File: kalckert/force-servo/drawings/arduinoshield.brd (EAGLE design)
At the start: 100 x 80 mm, 20 parts, among them IC1 MCP604P, IC2 7806L

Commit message: Finnished PC board
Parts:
- added X3, X4: (no value), con-phoenix-254:2POL254
- moved C1 33.2 mm to (56.1, 8.38), turned to 180 degrees
- moved SG1 30.9 mm to (40.4, 38.7), turned to 90 degrees
- moved C4 28.9 mm to (34.4, 8.38), turned to 90 degrees
- moved C3 28.6 mm to (45.7, 8.38), turned to 90 degrees
- moved C2 26.3 mm to (56.1, 21.5)
- moved POWERPIN 26.2 mm to (36.8, 2.54)
- moved IC2 26.0 mm to (40.0, 7.11)
- moved DIGITALPIN0-7 25.7 mm to (54.6, 50.8)
- moved DIGITALPIN8+ 25.6 mm to (30.2, 50.8)
- moved ANALOGPIN 25.3 mm to (57.1, 2.54)
- moved BATTERY 23.1 mm to (62.1, 9.91)
- moved 7905 20.3 mm to (57.4, 14.2), turned to 90 degrees
- moved X2 20.1 mm to (62.1, 29.5)
- moved X1 18.8 mm to (62.1, 23.1)
- moved SERVOPIN 15.1 mm to (63.5, 42.7)
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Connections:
- net GND: now also X3.1, X4.1
- net LED_GREEN: now also X3.2
- net LED_RED: now also X4.2
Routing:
- net GND: track 0.00 -> 151.0 mm
- net AMP_FORCE1: track 0.00 -> 77.6 mm
- net FORCE1: track 0.00 -> 62.4 mm
- net AMP_FORCE2: track 0.00 -> 57.5 mm
- net SERVOPOS: track 0.00 -> 52.8 mm, vias 0 -> 1
- net LED_RED: track 0.00 -> 49.8 mm
- net VCCSERVO: track 0.00 -> 48.5 mm
- net FORCE2: track 0.00 -> 46.0 mm
- net LED_GREEN: track 0.00 -> 45.9 mm
- net -9V: track 0.00 -> 42.3 mm
- net 5V: track 0.00 -> 39.2 mm
- net SERVOPWM: track 0.00 -> 37.7 mm
- net N$3: track 0.00 -> 18.7 mm
- net N$2: track 0.00 -> 16.3 mm
- net BUZZER: track 0.00 -> 10.4 mm
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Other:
- outline, holes or cut-outs redrawn

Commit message: First version of the PCB is ready.
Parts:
- removed 7905: 7905, linear:TO92
- removed IC2: 7806L, linear:TO92
- added IC3: 7806T, linear:TO220H
- added IC4: (no value), linear:TO220H
- moved R1 46.3 mm to (53.2, 12.6), turned to 90 degrees
- moved R4 39.7 mm to (15.2, 36.3), turned to 180 degrees
- moved R3 34.9 mm to (15.4, 42.7), turned to 180 degrees
- moved SERVOPIN 34.7 mm to (29.7, 34.8), turned to 180 degrees
- moved R2 32.7 mm to (50.7, 27.7), turned to 270 degrees
- moved C2 30.5 mm to (25.9, 17.3), turned to 90 degrees
- moved C1 30.4 mm to (25.9, 11.8), turned to 90 degrees
- moved C3 24.4 mm to (26.0, 22.9)
- moved C4 21.6 mm to (26.0, 28.3), turned to 270 degrees
- moved IC1 21.3 mm to (43.2, 20.1), turned to 90 degrees
- moved SG1 17.8 mm to (57.9, 41.7)
- moved BATTERY 3.06 mm to (62.4, 13.0)
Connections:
- net -9V: now also IC4.1; no longer 7905.1
- net BUZZER: now also DIGITALPIN0-7.4; no longer DIGITALPIN0-7.1
- net GND: now also IC4.3; no longer 7905.3
- net N$1: now also DIGITALPIN0-7.1; no longer DIGITALPIN0-7.3
- net N$2: now also IC4.2; no longer 7905.2
- net N$3: now also IC3.2; no longer IC2.2
- net N$4: now also DIGITALPIN0-7.2; no longer DIGITALPIN0-7.4
- net VCCSERVO: now also IC3.3; no longer IC2.1
- net VIN: now also IC3.1; no longer IC2.3
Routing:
- net N$4: track 5.89 -> 74.0 mm
- net AMP_FORCE1: track 77.6 -> 15.9 mm
- net VIN: track 5.08 -> 50.9 mm
- net LED_RED: track 49.8 -> 4.18 mm
- net LED_GREEN: track 45.9 -> 4.33 mm
- net FORCE1: track 62.4 -> 21.8 mm
- net -9V: track 42.3 -> 81.7 mm
- net VCCSERVO: track 48.5 -> 12.4 mm
- net FORCE2: track 46.0 -> 16.6 mm
- net N$2: track 16.3 -> 42.5 mm
- net N$1: track 5.65 -> 29.9 mm
- net SERVOPOS: track 52.8 -> 76.6 mm, vias 1 -> 0
- net AMP_FORCE2: track 57.5 -> 38.7 mm
- net 5V: track 39.2 -> 22.1 mm
- net N$3: track 18.7 -> 6.13 mm
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- added copper zone on layer 1, net N$8
- added copper zone on layer 16, net N$9
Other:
- board text added: "AlexDesign"

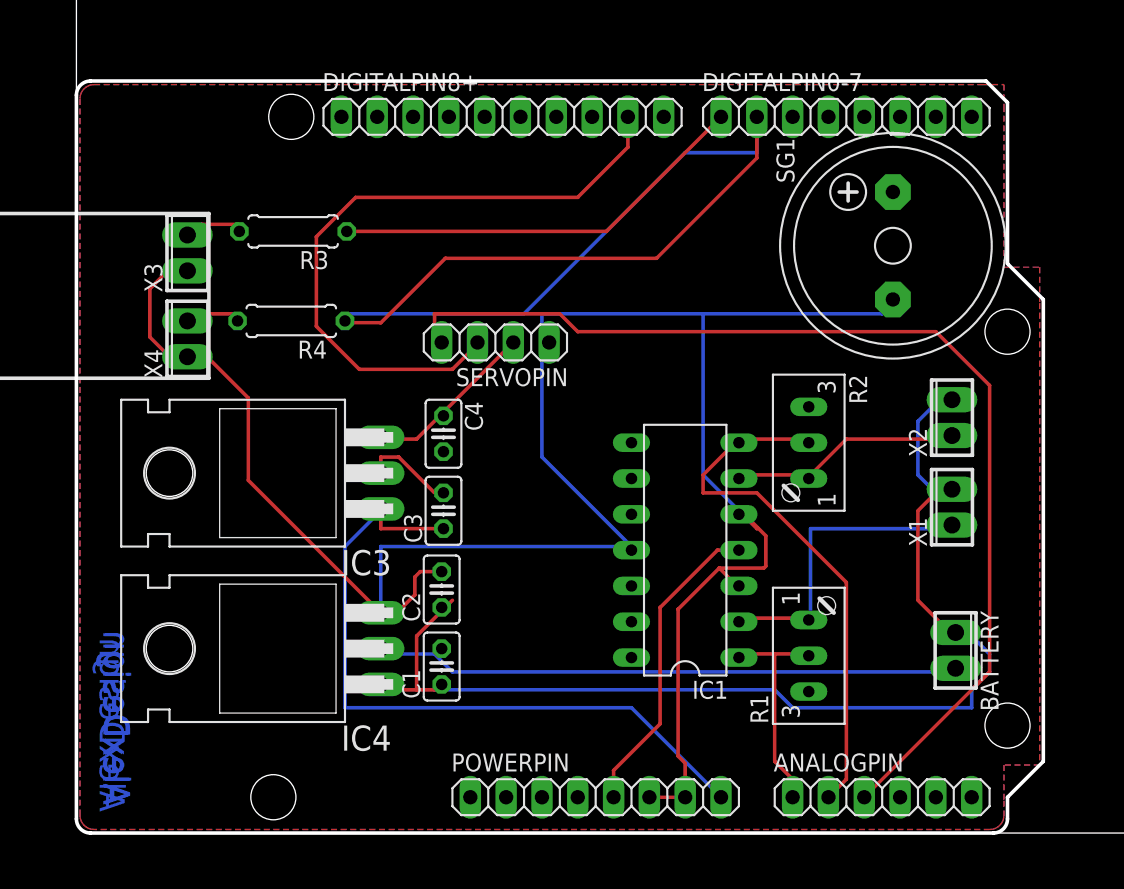
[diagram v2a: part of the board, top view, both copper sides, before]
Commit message: Added licensing info to board. Tested python program on mac (tkinter only works in IDLE).
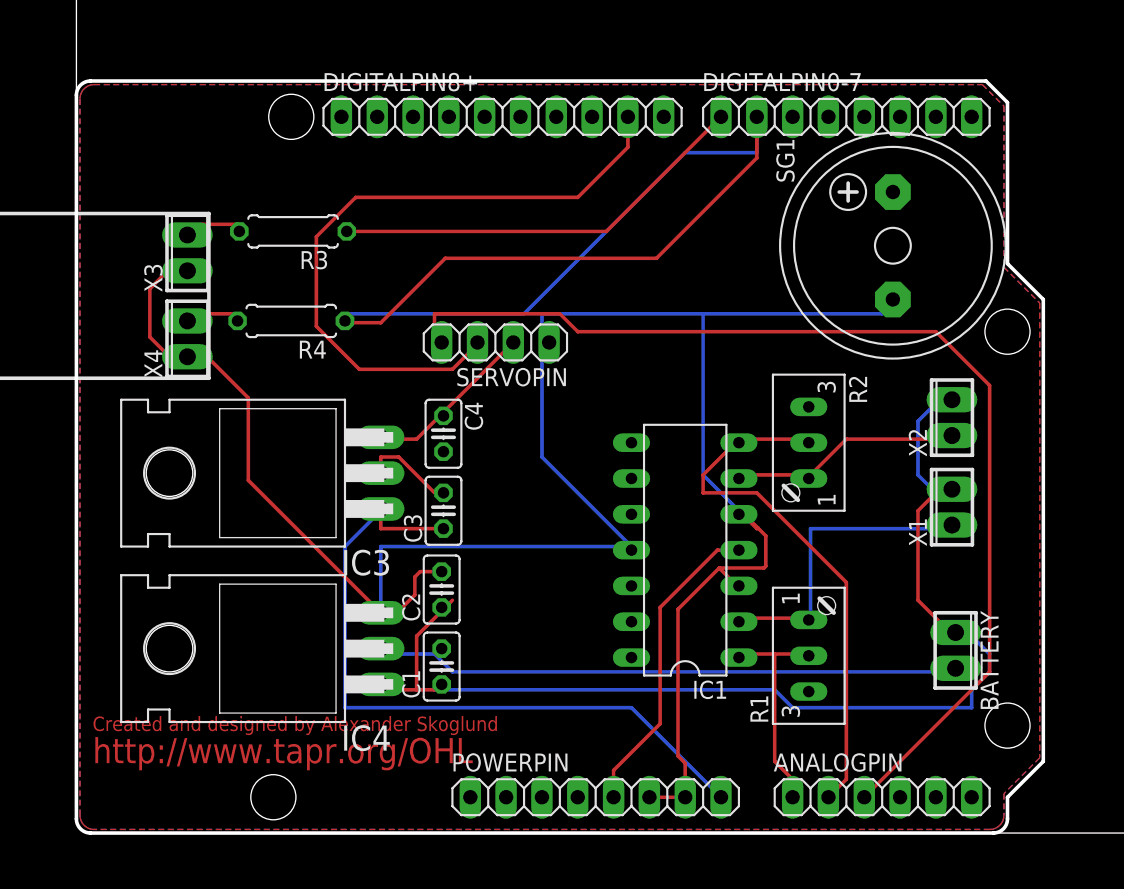
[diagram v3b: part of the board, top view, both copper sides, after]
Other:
- board text added: "Created and designed by Alexander Skoglund"
- board text added: "http://www.tapr.org/OHL"
- board text removed: "AlexDesign"
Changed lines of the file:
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@@
 <layer number="17" name="Pads" color="2" fill="1" visible="yes" active="yes"/>
 <layer number="18" name="Vias" color="2" fill="1" visible="yes" active="yes"/>
-<layer number="19" name="Unrouted" color="6" fill="1" visible="no" active="yes"/>
+<layer number="19" name="Unrouted" color="6" fill="1" visible="yes" active="yes"/>
 <layer number="20" name="Dimension" color="15" fill="1" visible="yes" active="yes"/>
-<layer number="21" name="tPlace" color="7" fill="1" visible="no" active="yes"/>
+<layer number="21" name="tPlace" color="7" fill="1" visible="yes" active="yes"/>
 <layer number="22" name="bPlace" color="7" fill="1" visible="no" active="yes"/>
-<layer number="23" name="tOrigins" color="15" fill="1" visible="no" active="yes"/>
-<layer number="24" name="bOrigins" color="15" fill="1" visible="no" active="yes"/>
-<layer number="25" name="tNames" color="7" fill="1" visible="no" active="yes"/>
-<layer number="26" name="bNames" color="7" fill="1" visible="no" active="yes"/>
+<layer number="23" name="tOrigins" color="15" fill="1" visible="yes" active="yes"/>
+<layer number="24" name="bOrigins" color="15" fill="1" visible="yes" active="yes"/>
+<layer number="25" name="tNames" color="7" fill="1" visible="yes" active="yes"/>
+<layer number="26" name="bNames" color="7" fill="1" visible="yes" active="yes"/>
 <layer number="27" name="tValues" color="7" fill="1" visible="no" active="yes"/>
 <layer number="28" name="bValues" color="7" fill="1" visible="no" active="yes"/>
@@
 <wire x1="9.398" y1="32.258" x2="-6.35" y2="32.258" width="0.254" layer="21"/>
 <wire x1="-6.35" y1="32.258" x2="-6.35" y2="43.942" width="0.254" layer="21"/>
-<text x="3.81" y="14.351" size="1.778" layer="16" rot="MR270">AlexDesign</text>
-<text x="3.683" y="14.351" size="1.778" layer="16" rot="MR270">AlexDesign</text>
-<text x="3.429" y="13.843" size="1.778" layer="16" rot="MR270">AlexDesign</text>
+<text x="1.143" y="4.953" size="1.778" layer="1">http://www.tapr.org/OHL</text>
+<text x="1.143" y="7.239" size="1.016" layer="1">Created and designed by Alexander Skoglund</text>
 </plain>
 <attributes>
@@
 <vertex x="1.254" y="53.086"/>
 <vertex x="64.262" y="53.086"/>
-<vertex x="65.786" y="53.086"/>
 <vertex x="65.786" y="51.562"/>
 <vertex x="65.786" y="40.132"/>
-<vertex x="68.326" y="40.132"/>
 <vertex x="68.326" y="37.592"/>
-<vertex x="68.326" y="4.826"/>
-<vertex x="65.786" y="4.826"/>
-<vertex x="65.786" y="2.286"/>
+<vertex x="68.326" y="5.334"/>
+<vertex x="65.786" y="2.794"/>
 <vertex x="65.786" y="1.254" curve="-90"/>
 <vertex x="64.786" y="0.254"/>
@@
 <vertex x="1.254" y="53.086"/>
 <vertex x="64.262" y="53.086"/>
-<vertex x="65.786" y="53.086"/>
 <vertex x="65.786" y="51.562"/>
 <vertex x="65.786" y="40.132"/>
-<vertex x="68.326" y="40.132"/>
 <vertex x="68.326" y="37.592"/>
-<vertex x="68.326" y="4.826"/>
-<vertex x="65.786" y="4.826"/>
-<vertex x="65.786" y="2.286"/>
+<vertex x="68.326" y="5.334"/>
+<vertex x="65.786" y="2.794"/>
 <vertex x="65.786" y="1.254" curve="-90"/>
 <vertex x="64.786" y="0.254"/>

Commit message: Added a timestamp to the measure, ms from start of prog.
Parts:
- added SG2: EFBRD22C41, buzzer:EFBRD22C41
- added SG3: EFBAA40D101, buzzer:EFBAA40D101
- added SG4: F/QMX, buzzer:F/QMX
- added SG5: EFBRD22C413, buzzer:EFBRD22C413
- added SG6: EFBRD24C411, buzzer:EFBRD24C411
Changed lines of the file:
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@@
 <element name="IC3" library="linear" package="TO220H" value="7806T" x="11.43" y="25.527" rot="R90"/>
 <element name="IC4" library="linear" package="TO220H" value="" x="11.43" y="13.081" rot="R90"/>
+<element name="SG4" library="buzzer" package="F/QMX" value="F/QMX" x="80.137" y="59.69" rot="R90">
+<attribute name="OC_NEWARK" value="unknown" x="80.137" y="59.69" size="1.778" layer="27" rot="R90" display="off"/>
+<attribute name="MPN" value="" x="80.137" y="59.69" size="1.778" layer="27" rot="R90" display="off"/>
+<attribute name="MF" value="" x="80.137" y="59.69" size="1.778" layer="27" rot="R90" display="off"/>
+<attribute name="OC_FARNELL" value="unknown" x="80.137" y="59.69" size="1.778" layer="27" rot="R90" display="off"/>
+</element>
+<element name="SG2" library="buzzer" package="EFBRD22C41" value="EFBRD22C41" x="4.572" y="-11.176">
+<attribute name="OC_NEWARK" value="unknown" x="4.572" y="-11.176" size="1.778" layer="27" display="off"/>
+<attribute name="MPN" value="" x="4.572" y="-11.176" size="1.778" layer="27" display="off"/>
+<attribute name="MF" value="" x="4.572" y="-11.176" size="1.778" layer="27" display="off"/>
+<attribute name="OC_FARNELL" value="unknown" x="4.572" y="-11.176" size="1.778" layer="27" display="off"/>
+</element>
+<element name="SG3" library="buzzer" package="EFBAA40D101" value="EFBAA40D101" x="2.032" y="-30.734">
+<attribute name="OC_NEWARK" value="unknown" x="2.032" y="-30.734" size="1.778" layer="27" display="off"/>
+<attribute name="MPN" value="" x="2.032" y="-30.734" size="1.778" layer="27" display="off"/>
+<attribute name="MF" value="" x="2.032" y="-30.734" size="1.778" layer="27" display="off"/>
+<attribute name="OC_FARNELL" value="unknown" x="2.032" y="-30.734" size="1.778" layer="27" display="off"/>
+</element>
+<element name="SG5" library="buzzer" package="EFBRD22C413" value="EFBRD22C413" x="4.572" y="-50.292">
+<attribute name="OC_NEWARK" value="unknown" x="4.572" y="-50.292" size="1.778" layer="27" display="off"/>
+<attribute name="MPN" value="" x="4.572" y="-50.292" size="1.778" layer="27" display="off"/>
+<attribute name="MF" value="" x="4.572" y="-50.292" size="1.778" layer="27" display="off"/>
+<attribute name="OC_FARNELL" value="unknown" x="4.572" y="-50.292" size="1.778" layer="27" display="off"/>
+</element>
+<element name="SG6" library="buzzer" package="EFBRD24C411" value="EFBRD24C411" x="5.588" y="-73.406">
+<attribute name="OC_NEWARK" value="unknown" x="5.588" y="-73.406" size="1.778" layer="27" display="off"/>
+<attribute name="MPN" value="" x="5.588" y="-73.406" size="1.778" layer="27" display="off"/>
+<attribute name="MF" value="" x="5.588" y="-73.406" size="1.778" layer="27" display="off"/>
+<attribute name="OC_FARNELL" value="unknown" x="5.588" y="-73.406" size="1.778" layer="27" display="off"/>
+</element>
 </elements>
 <signals>

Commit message: Added hardware licensing files. Updated shematic to prevent autoreset of Arduino.
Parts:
- removed SG2: EFBRD22C41, buzzer:EFBRD22C41
- removed SG3: EFBAA40D101, buzzer:EFBAA40D101
- removed SG5: EFBRD22C413, buzzer:EFBRD22C413
- removed SG6: EFBRD24C411, buzzer:EFBRD24C411
- added C5: 10uF, resistor:C025-025X050
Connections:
- new net RESET: C5.1, POWERPIN.1
- net GND: now also C5.2
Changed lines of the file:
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@@
 <attribute name="OC_FARNELL" value="unknown" x="80.137" y="59.69" size="1.778" layer="27" rot="R90" display="off"/>
 </element>
-<element name="SG2" library="buzzer" package="EFBRD22C41" value="EFBRD22C41" x="4.572" y="-11.176">
-<attribute name="OC_NEWARK" value="unknown" x="4.572" y="-11.176" size="1.778" layer="27" display="off"/>
-<attribute name="MPN" value="" x="4.572" y="-11.176" size="1.778" layer="27" display="off"/>
-<attribute name="MF" value="" x="4.572" y="-11.176" size="1.778" layer="27" display="off"/>
-<attribute name="OC_FARNELL" value="unknown" x="4.572" y="-11.176" size="1.778" layer="27" display="off"/>
-</element>
-<element name="SG3" library="buzzer" package="EFBAA40D101" value="EFBAA40D101" x="2.032" y="-30.734">
-<attribute name="OC_NEWARK" value="unknown" x="2.032" y="-30.734" size="1.778" layer="27" display="off"/>
-<attribute name="MPN" value="" x="2.032" y="-30.734" size="1.778" layer="27" display="off"/>
-<attribute name="MF" value="" x="2.032" y="-30.734" size="1.778" layer="27" display="off"/>
-<attribute name="OC_FARNELL" value="unknown" x="2.032" y="-30.734" size="1.778" layer="27" display="off"/>
-</element>
-<element name="SG5" library="buzzer" package="EFBRD22C413" value="EFBRD22C413" x="4.572" y="-50.292">
-<attribute name="OC_NEWARK" value="unknown" x="4.572" y="-50.292" size="1.778" layer="27" display="off"/>
-<attribute name="MPN" value="" x="4.572" y="-50.292" size="1.778" layer="27" display="off"/>
-<attribute name="MF" value="" x="4.572" y="-50.292" size="1.778" layer="27" display="off"/>
-<attribute name="OC_FARNELL" value="unknown" x="4.572" y="-50.292" size="1.778" layer="27" display="off"/>
-</element>
-<element name="SG6" library="buzzer" package="EFBRD24C411" value="EFBRD24C411" x="5.588" y="-73.406">
-<attribute name="OC_NEWARK" value="unknown" x="5.588" y="-73.406" size="1.778" layer="27" display="off"/>
-<attribute name="MPN" value="" x="5.588" y="-73.406" size="1.778" layer="27" display="off"/>
-<attribute name="MF" value="" x="5.588" y="-73.406" size="1.778" layer="27" display="off"/>
-<attribute name="OC_FARNELL" value="unknown" x="5.588" y="-73.406" size="1.778" layer="27" display="off"/>
-</element>
+<element name="C5" library="resistor" package="C025-025X050" value="10uF" x="-3.683" y="-3.429"/>
 </elements>
 <signals>
@@
 <wire x1="39.37" y1="20.32" x2="39.37" y2="20.066" width="0.254" layer="16"/>
 <wire x1="21.59" y1="15.24" x2="21.59" y2="15.621" width="0.254" layer="16"/>
+<contactref element="C5" pad="2"/>
+<wire x1="-2.413" y1="-3.429" x2="21.59" y2="15.24" width="0" layer="19" extent="16-16"/>
 </signal>
 <signal name="VCCSERVO">
@@
 </polygon>
 </signal>
+<signal name="RESET">
+<contactref element="POWERPIN" pad="1"/>
+<contactref element="C5" pad="1"/>
+<wire x1="-4.953" y1="-3.429" x2="27.94" y2="2.54" width="0" layer="19" extent="1-1"/>
+</signal>
 </signals>
